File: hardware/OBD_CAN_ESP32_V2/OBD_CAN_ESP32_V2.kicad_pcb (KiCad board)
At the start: 2 copper layers, 61.5 x 30 mm, 39 parts, among them J1 OBD-II INPUT, J3 ESP32_S3_DEVKITC_J1, J4 ESP32_S3_DEVKITC_J3, Q1 Q_PMOS_GDS, U1 SN65HVD230, U2 TPS54360BDDA

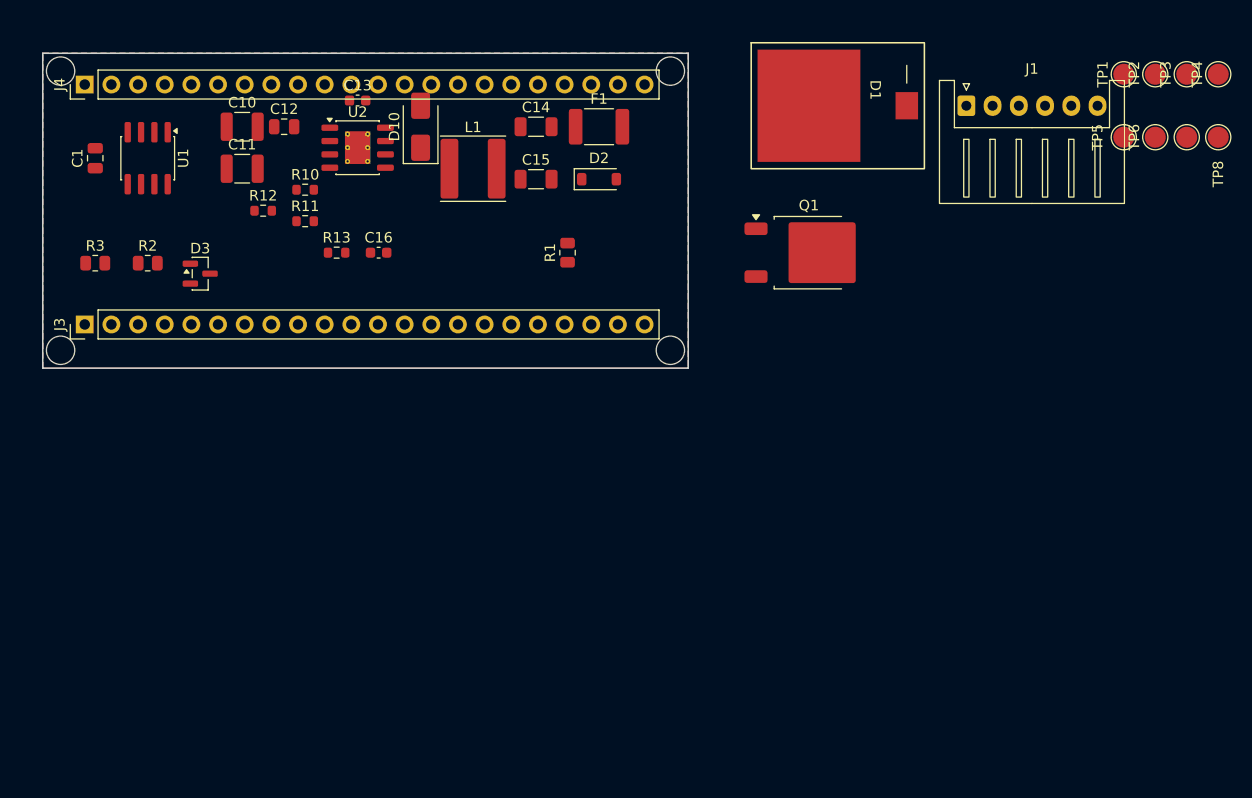
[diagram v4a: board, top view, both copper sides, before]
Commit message: hardware: V2 64x31 재배치 — 커트야드 기준 자동 간격분리 (겹침 0)
- 보드 61.5x30 → 64x31 (나사구멍·헤더 간격 여유)
- 앞면 SMD 커트야드 겹침 0, 헤더행/나사구멍 침범 0 (자동 분리 알고리즘)
- 뒷면(D1/Q1/J1/TP) 사용자 배치 보존

Co-Authored-By: Claude Fable 5 <noreply@anthropic.com>
Claude-Session: https://claude.ai/code/session_015Lj2iN8K2AKiUuQKmtXaeP
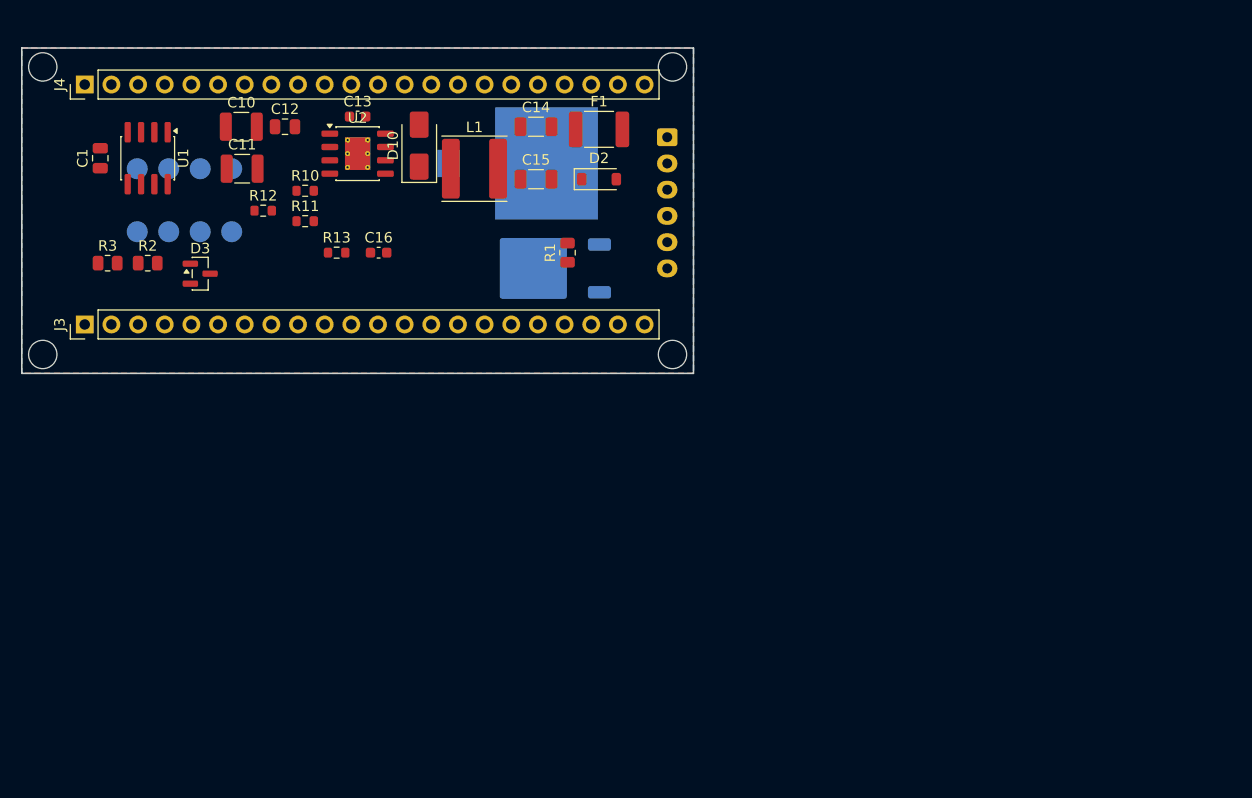
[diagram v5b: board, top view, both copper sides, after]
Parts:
- D1, J1, Q1, TP1, TP2, TP3, TP4, TP5, TP6, TP7, TP8: moved to B.Cu
- moved TP4 103.4 mm to (66.0, 102.0)
- moved TP8 103.4 mm to (66.0, 108.0)
- moved TP3 97.4 mm to (69.0, 102.0)
- moved TP7 97.4 mm to (69.0, 108.0)
- moved TP2 91.4 mm to (72.0, 102.0)
- moved TP6 91.4 mm to (72.0, 108.0)
- moved TP1 85.5 mm to (75.0, 102.0)
- moved TP5 85.5 mm to (75.0, 108.0)
- moved J1 28.7 mm to (116.5, 99.0), turned to -90 degrees
- moved D1 25.6 mm to (105.0, 101.5), turned to 180 degrees
- moved Q1 25.0 mm to (105.0, 111.5), turned to 180 degrees
- moved D10 1.80 mm to (92.9, 99.8)
- moved H1 1.75 mm to (57.0, 92.3)
- moved H3 1.75 mm to (57.0, 119.7)
- moved C13 1.53 mm to (87.0, 97.0)
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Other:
- board size 61.5 x 30 mm -> 64 x 31 mm

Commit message: hardware: V2 64x36 최종 — 나사구멍 헤더 밖 배치 + 최소홀 0.2mm
- 보드 64x31 → 64x36 (헤더 위/아래 여백 확보)
- 나사구멍 4개를 헤더 커트야드 밖 상하 코너로 (겹침 0)
- 보드 최소 through-hole 0.3 → 0.2mm (U2 TPS54360B 열패드 방열비아 12개 허용, JLCPCB 지원)

Co-Authored-By: Claude Fable 5 <noreply@anthropic.com>
Claude-Session: https://claude.ai/code/session_015Lj2iN8K2AKiUuQKmtXaeP
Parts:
- moved H1 2.88 mm to (58.0, 89.6)
- moved H2 2.88 mm to (116.0, 89.6)
- moved H3 2.88 mm to (58.0, 122.4)
- moved H4 2.88 mm to (116.0, 122.4)
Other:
- board size 64 x 31 mm -> 64 x 36 mm
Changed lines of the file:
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@@
 	(footprint "MountingHole:MountingHole_2.7mm_M2.5"
 		(layer "F.Cu")
-		(at 57 92.3)
+		(at 58 89.6)
 		(property "Reference" "H1"
 			(at 0 -3 0)
@@
 	(footprint "MountingHole:MountingHole_2.7mm_M2.5"
 		(layer "F.Cu")
-		(at 117 119.7)
+		(at 116 122.4)
 		(property "Reference" "H4"
 			(at 0 -3 0)
@@
 	(footprint "MountingHole:MountingHole_2.7mm_M2.5"
 		(layer "F.Cu")
-		(at 117 92.3)
+		(at 116 89.6)
 		(property "Reference" "H2"
 			(at 0 -3 0)
@@
 	(footprint "MountingHole:MountingHole_2.7mm_M2.5"
 		(layer "F.Cu")
-		(at 57 119.7)
+		(at 58 122.4)
 		(property "Reference" "H3"
 			(at 0 -3 0)
@@
 	)
 	(gr_rect
-		(start 55 90.5)
-		(end 119 121.5)
+		(start 55 88)
+		(end 119 124)
 		(stroke
 			(width 0.15)
@@
 		(polygon
 			(pts
-				(xy 55 90.5) (xy 119 90.5) (xy 119 121.5) (xy 55 121.5)
+				(xy 55 88) (xy 119 88) (xy 119 124) (xy 55 124)
 			)
 		)
@@
 		(polygon
 			(pts
-				(xy 55 90.5) (xy 119 90.5) (xy 119 121.5) (xy 55 121.5)
+				(xy 55 88) (xy 119 88) (xy 119 124) (xy 55 124)
 			)
 		)
